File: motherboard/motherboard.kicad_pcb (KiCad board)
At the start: 2 copper layers, 82 x 54.8 mm, 70 parts, among them J1 locked, J10 Programmer, J3 Battery / Pitot/ Orientation, J4 c02 censor, J5 shaftencorder, J6 USB_C_Receptacle_USB2.0, J7 SparLoad, J8 lidar, J9 Control Board, Q1 2N7002K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

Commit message: Updated with Savo's suggested changes
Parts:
- removed J10: Programmer, Connector_PinHeader_1.27mm:PinHeader_2x07_P1.27mm_Vertical_SMD
- removed JP2: opamp out, Jumper:SolderJumper-2_P1.3mm_Open_RoundedPad1.0x1.5mm
- removed JP3: op-amp bypass, Jumper:SolderJumper-2_P1.3mm_Open_RoundedPad1.0x1.5mm
- removed R2: 10k, Resistor_SMD:R_0603_1608Metric
- added J2: Conn_ST_STDC14, Connector_PinHeader_1.27mm:PinHeader_2x07_P1.27mm_Vertical_SMD, F.Cu at (77.3, 83.1)
- C13: value 100n -> 0.22u
- JP1: value BOOT0 -> Jumper_3_Open
- moved JP1 28.9 mm to (91.9, 90.2)
- moved C6 0.76 mm to (104.6, 89.9)
- moved Q1 0.57 mm to (102.6, 81.5)
- moved C5 0.51 mm to (104.6, 85.6)
- moved U5 0.35 mm to (113.3, 111.5)
- moved J8 0.21 mm to (129.9, 111.5)
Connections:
- C15 pad 1: /SHAFTENC -> /SHAFTENC IN
- J5 pad 2: /SHAFTENC -> /SHAFTENC IN
- JP1 pad 1: GND -> /SHAFTENC IN
- JP1 pad 2: /BOOT0 -> /SHAFTENC OUT
- JP1 pad 3: +3.3V -> Net-(JP1-B)
- R17 pad 2: /SHAFTENC -> /SHAFTENC IN
- U3 pad 1: Net-(JP2-A) -> Net-(JP1-B)
- U3 pad 3: /SHAFTENC -> /SHAFTENC IN
- U6 pad 60: /BOOT0 -> GND
- U6 pad 61: /RPM -> /SHAFTENC OUT
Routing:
- net /USART2_{RX}: track 0.00 -> 32.2 mm
- net /USART2_{TX}: track 0.00 -> 31.6 mm, vias 0 -> 2
- net /RPM: track 29.1 -> 0.00 mm, vias 2 -> 0
- net /SHAFTENC IN: track 0.00 -> 29.0 mm, vias 0 -> 2
- net /SHAFTENC: track 28.8 -> 0.00 mm, vias 2 -> 0
- net /SHAFTENC OUT: track 0.00 -> 27.3 mm, vias 0 -> 2
- net Net-(JP1-B): track 0.00 -> 12.7 mm, vias 0 -> 2
- net Net-(JP2-A): track 11.8 -> 0.00 mm, vias 2 -> 0
- net /BOOT0: track 9.20 -> 0.00 mm
- net /SPI1SCK: track 92.3 -> 93.5 mm
- net +5V: track 215.4 -> 216.5 mm
- net /SPI1MISO: track 83.2 -> 83.9 mm
- net +3.3V: track 29.3 -> 29.1 mm, vias 14 -> 13
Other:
- board text added: "3V3"
- board text removed: "3.3V"

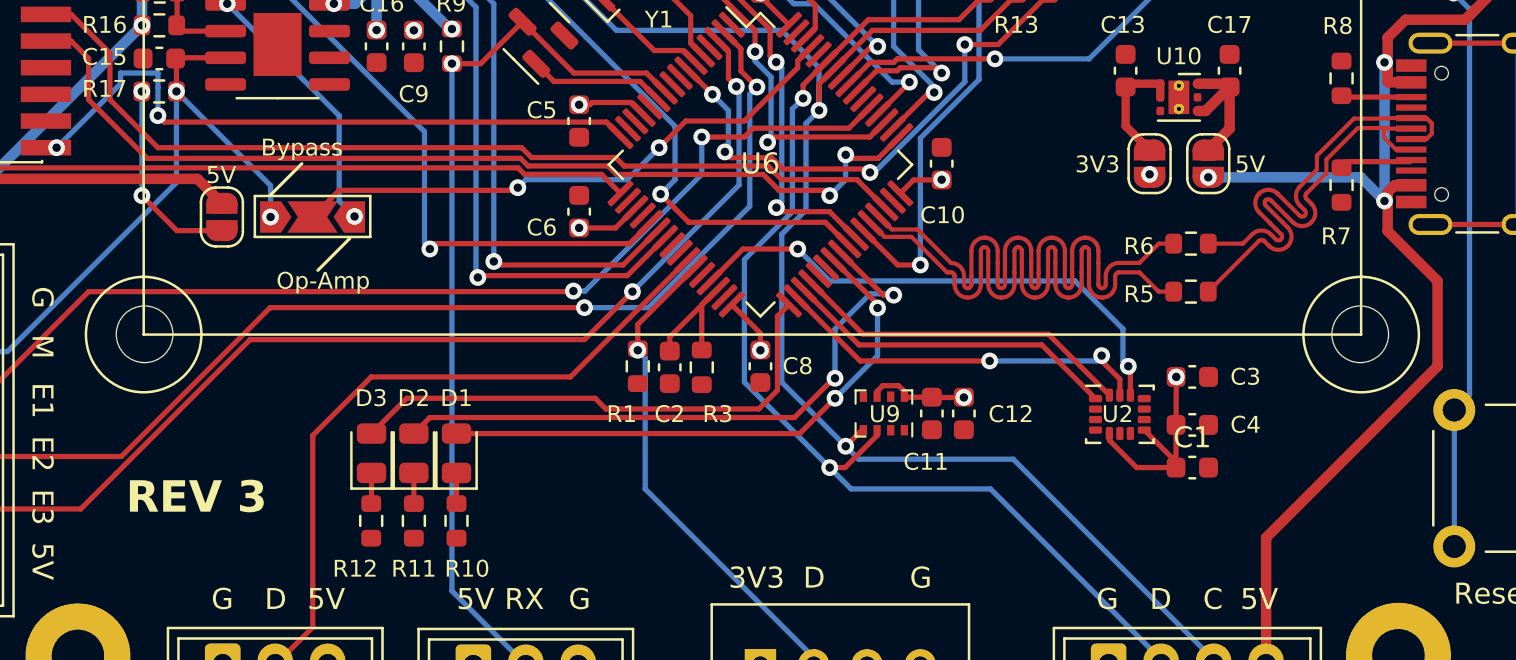
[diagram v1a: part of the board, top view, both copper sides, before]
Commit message: Updated schematic symbols
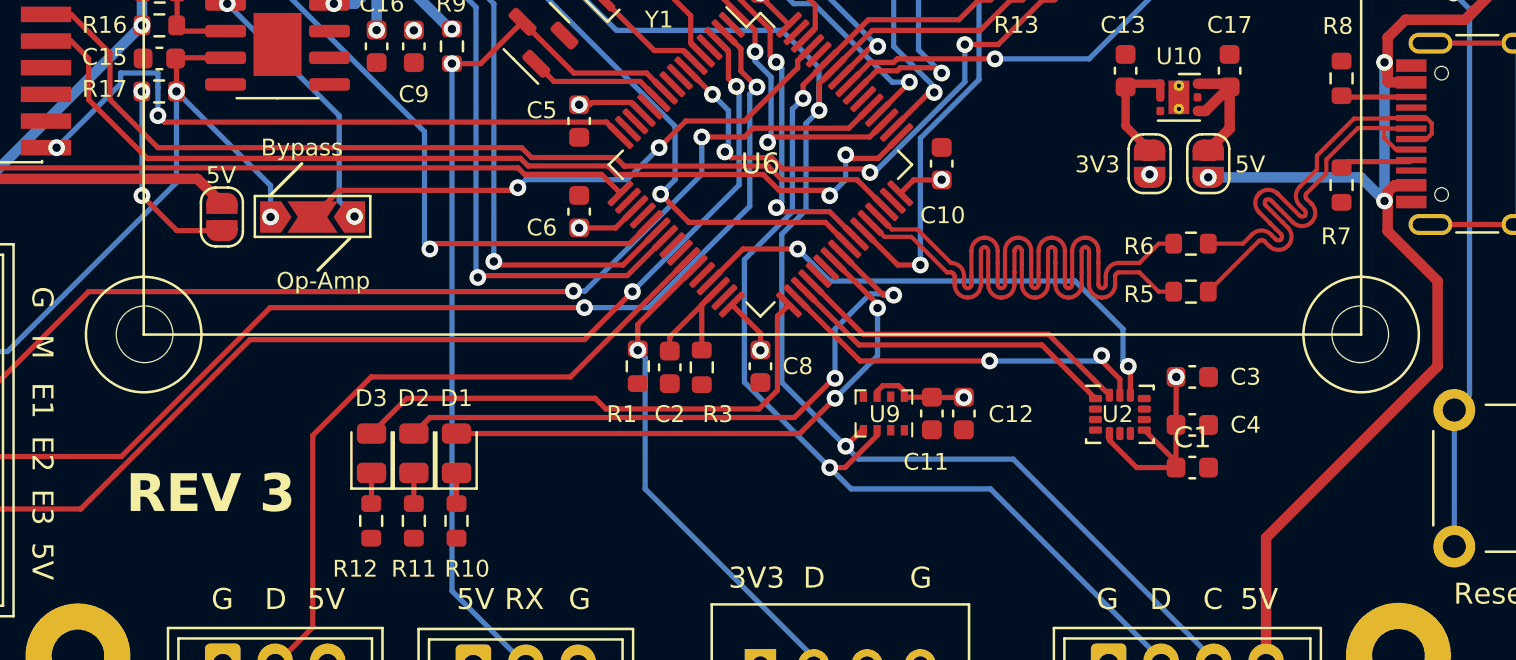
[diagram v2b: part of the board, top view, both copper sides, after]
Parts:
- J1: value locked -> Raspberry_Pi_2_3 ANT

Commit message: Changed voltage regulator footprint
Removed thermal vias since they were too small for manufacturing.
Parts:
- U10: footprint Package_SON:WSON-6-1EP_2x2mm_P0.65mm_EP1x1.6mm_ThermalVias -> Package_SON:WSON-6-1EP_2x2mm_P0.65mm_EP1x1.6mm
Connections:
- U6 pad 37: /USART6_{TX} -> unconnected-(U6-PC6-Pad37)
- U6 pad 38: /USART6_{RX} -> unconnected-(U6-PC7-Pad38)
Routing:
- net unconnected-(J6-SHIELD-PadS1)_0: track 17.0 -> 0.00 mm
